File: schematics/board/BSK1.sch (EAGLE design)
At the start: 29 parts

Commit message: Сделаны платы CROSSnew, SPIDERnew, BSK2
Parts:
- removed BSK3: (no value), pinheadCS:PINHD-1X8
- added BKU: (no value), pinheadCS:PINHD-1X20
- added CMD: KCONNECTQUAD, CanCubeSat:KCONNECTQUAD
- added JP1, JP2, JP3, JP4, JP5, JP6: (no value), pinheadCS:PINHD-2X10
- added U$16, U$17, U$6, U$7: GRAFITGRAFIT3_1, CanCubeSat:GRAFITGRAFIT3_1
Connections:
- removed net B5-KHEAT: R8.1, U$8.G
- removed net B5-KVCC: R94.2, R95.2, U$5.AN1, U$5.AN2
- removed net B5-ROZE: R14.1, U$13.G
- removed net KEM7: BSK3.3
- removed net KEM8: BSK3.2
- removed net KHEAT4: BSK3.4
- removed net KVCC4: BSK3.5
- new net 3V3: BKU.8, JP1.9, JP2.9, JP3.9, JP4.9, JP5.9, JP6.9
- new net B1-CMD: BKU.4, CMD.P$1
- new net B1-KHEAT: BKU.1, R8.1, U$8.G
- new net B1-KVCC: BKU.2, R94.2, R95.2, U$5.AN1, U$5.AN2
- new net B1-ROZE: BKU.3, R14.1, U$13.G
- new net BMS1: JP1.1, JP2.1, JP3.1, JP4.5, JP5.3, JP6.3
- new net BMS2: JP1.2, JP2.2, JP3.2, JP4.6, JP5.4, JP6.4
- new net BMS3: JP1.3, JP2.3, JP3.3, JP4.1, JP5.5, JP6.5
- new net BMS4: JP1.4, JP2.4, JP3.4, JP4.2, JP5.6, JP6.6
- new net BMS5: JP1.5, JP2.5, JP3.5, JP4.3, JP5.1, JP6.1
- new net BMS6: JP1.6, JP2.6, JP3.6, JP4.4, JP5.2, JP6.2
- new net I2CINT: BKU.13
- new net INT: JP1.16, JP2.16, JP3.16, JP4.16, JP5.16, JP6.16
- new net PL1: JP1.17, JP2.17, JP3.17, JP4.17, JP5.17, JP6.17
- new net PL1-KVCC: BKU.15
- new net PL2: JP1.19, JP2.19, JP3.19, JP4.19, JP5.19, JP6.19
- new net PL2-KVCC: BKU.16
- new net PL3: JP1.18, JP2.18, JP3.18, JP4.18, JP5.18, JP6.18
- new net PL3-KVCC: BKU.17
- new net PL4: JP1.20, JP2.20, JP3.20, JP4.20, JP5.20, JP6.20
- new net PL4-KVCC: BKU.18
- new net PL5-KVCC: BKU.19
- new net PL6-KVCC: BKU.20
- new net SCL: BKU.10, JP1.13, JP2.13, JP3.13, JP4.13, JP5.13, JP6.13
- new net SDA: BKU.12, JP1.14, JP2.14, JP3.14, JP4.14, JP5.14, JP6.14
- new net TIME: BKU.14, JP1.15, JP2.15, JP3.15, JP4.15, JP5.15, JP6.15
- net 1W: now also BKU.5, JP1.7, JP2.7, JP3.7, JP4.7, JP5.7, JP6.7; no longer BSK3.6
- net 2: now also U$16.P$1, U$17.P$1, U$6.P$1, U$7.P$1
- net 5V: now also BKU.7, JP1.10, JP2.10, JP3.10, JP4.10, JP5.10, JP6.10; no longer BSK3.7
- net BUS+: now also BKU.6, JP1.8, JP2.8, JP3.8, JP4.8, JP5.8, JP6.8, U$16.P$2, U$17.P$2, U$6.P$2, U$7.P$2; no longer BSK3.8
- net GND: now also BKU.11, BKU.9, JP1.11, JP1.12, JP2.11, JP2.12, JP3.11, JP3.12, JP4.11, JP4.12, JP5.11, JP5.12, JP6.11, JP6.12; no longer BSK3.1
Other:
- moved on the sheet: LAP1, LED6, LED7, R12, R13, R14, R4, R5, R6, R7, R8, R9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

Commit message: Добавлены предохранители в библиотеку
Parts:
- removed U$11, U$12: KCONNECT, CanCubeSat:KCONNECT
- removed U$26: FS8205A+, CanCubeSat:FS8205A+
- added BSK5: (no value), pinheadCS:PINHD-1X8
- added LED-G1, LED-G2, LED-G3, LED-G4, LED-G5, LED-G6: (no value), led:LEDCHIPLED_0603
- added R10, R11, R15, R16, R17, R21, R22, R23: 2k, resistor:R-US_R0603
- added R18, R20, R3: 1M, resistor:R-US_R0603
- added R19: 1k5, resistor:R-US_R0603
- added U$18, U$19, U$20, U$21: KCONNECT, CanCubeSat:KCONNECT
- added U$22: MOCD217M, CanCubeSat:MOCD217M
- added U$23: SI2302CDS, CanCubeSat:SI2302CDS
- added U$27, U$28, U$30: GRAFITGRAFIT3_1, CanCubeSat:GRAFITGRAFIT3_1
- R12, R6: value 2M -> 1M
- R13: value 1k5 -> 1M
- R4, R7: value 2k -> 2M
- U$10, U$9: value KCONNECT -> SI2302CDS; device CanCubeSat:KCONNECT -> CanCubeSat:SI2302CDS
- U$17: value GRAFITGRAFIT3_1 -> FS8205A+; device CanCubeSat:GRAFITGRAFIT3_1 -> CanCubeSat:FS8205A+
- U$5: value MOCD217M -> SI2302CDS; device CanCubeSat:MOCD217M -> CanCubeSat:SI2302CDS
- U$6, U$7: value GRAFITGRAFIT3_1 -> SI2302CDS; device CanCubeSat:GRAFITGRAFIT3_1 -> CanCubeSat:SI2302CDS
- renumbered LAP1 to LED_Y, LED6 to LED_B1, LED7 to LED_R, R94 to R1, R95 to R2, U$13 to U$25, U$14 to U$24, U$16 to U$29
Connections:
- removed net 1: R7.2, U$24.GND, U$8.D
- removed net 2: R13.2, U$17.P$1, U$25.D, U$29.P$1, U$6.P$1, U$7.P$1
- removed net I2CINT: BKU.13
- removed net N$26: R5.1, R6.2, U$26.G2
- removed net N$29: LED_R.C, R13.1
- removed net N$31: LED_B1.C, R7.1
- removed net OC1: R9.2, U$5.COL2
- removed net OD1: R5.2, U$5.COL1
- new net 3: R11.2, U$23.D, U$24.GND
- new net 4: R19.2, U$25.D, U$27.P$1, U$28.P$1, U$29.P$1, U$30.P$1
- new net N$2: LED_B1.C, R11.1
- new net N$21: LED-G3.A, R17.2
- new net N$22: LED-G4.A, R21.2
- new net N$23: LED-G5.A, R22.2
- new net N$24: LED-G6.A, R23.2
- new net N$3: LED_R.C, R19.1
- new net N$38: LED-G2.A, R15.2
- new net N$4: LED-G1.A, R16.2
- new net OC2: R3.2, U$22.COL2
- new net OD2: R5.2, U$22.COL1
- new net PL1-GND: JP1.11, JP1.12, LED-G1.C, U$5.D
- new net PL2-GND: JP2.11, JP2.12, LED-G2.C, U$6.D
- new net PL3-GND: JP3.11, JP3.12, LED-G3.C, U$7.D
- new net PL4-GND: JP4.11, JP4.12, LED-G4.C, U$8.D
- new net PL5-GND: JP5.11, JP5.12, LED-G5.C, U$9.D
- new net PL6-GND: JP6.11, JP6.12, LED-G6.C, U$10.D
- new net TIME-ES: BKU.13, BSK5.8
- net 3V3: now also BSK5.3
- net 5V: now also BSK5.2, R10.1, R15.1, R16.1, R17.1, R21.1, R22.1, R23.1; no longer R4.1
- net B1-KHEAT: now also R18.1, U$23.G; no longer R8.1, U$8.G
- net B1-KVCC: now also U$22.AN1, U$22.AN2; no longer U$5.AN1, U$5.AN2
- net B1-ROZE: now also R20.1; no longer R14.1
- net BUS+: now also R4.1, R7.2, U$27.P$2, U$28.P$2, U$30.P$2; no longer R12.2, R6.1, U$17.P$2, U$6.P$2, U$7.P$2
- net BUS+2: now also U$18.P$1; no longer U$9.P$1
- net BUS+3: now also U$20.P$1; no longer U$11.P$1
- net BUS-: now also U$17.S2, U$22.EM1; no longer U$26.S2, U$5.EM1
- net BUS-2: now also U$19.P$1; no longer U$10.P$1
- net BUS-3: now also U$21.P$1; no longer U$12.P$1
- net GND: now also BSK5.1, BSK5.4, BSK5.6, DS18B20Z.HEAT, R12.2, R13.2, R18.2, R20.2, R6.2, R9.2, U$10.S, U$17.HEAT, U$17.S1, U$22.CAT1, U$22.CAT2, U$22.EM2, U$23.S, U$5.S, U$6.S, U$7.S, U$9.S; no longer JP1.11, JP1.12, JP2.11, JP2.12, JP3.11, JP3.12, JP4.11, JP4.12, JP5.11, JP5.12, JP6.11, JP6.12, U$26.S1, U$5.CAT1, U$5.CAT2, U$5.EM2
- net N$1: now also R4.2, R5.1, U$17.G2; no longer DS18B20Z.HEAT, U$26.HEAT
- net N$27: now also R3.1, R7.1, U$17.G1; no longer R12.1, R9.1, U$26.G1
- net N$28: now also R10.2; no longer R4.2
- net PL1-KVCC: now also R6.1, U$5.G
- net PL2-KVCC: now also R8.1, U$6.G
- net PL3-KVCC: now also R9.1, U$7.G
- net PL4-KVCC: now also R12.1, U$8.G
- net PL5-KVCC: now also R13.1, U$9.G
- net PL6-KVCC: now also R14.1, U$10.G
- net SCL: now also BSK5.5
- net SDA: now also BSK5.7
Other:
- moved on the sheet: R12, R13, R14, R4, R6, R7, R8, R9, U$1, U$2, U$3, U$4

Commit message: Разведена БСК1
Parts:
- added C41: 0,1µ, rcl:C-USC0603
- added R75: R01, rcl:R-US_R2512
- added R76, R77: 10R, resistor:R-US_R0603
- added U$57: INA219AID, CanCubeSat:INA219AID
- BSK5: device pinheadCS:PINHD-1X8 -> pinheadCS:PINHD-1X10
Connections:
- net BUS+1 renamed SP+1
- net BUS+2 renamed SP+3
- net BUS- renamed SP-
- net BUS-1 renamed SP-1
- net BUS-2 renamed SP-2
- net BUS-3 renamed SP-3
- net SCL renamed SCL-TM
- net SDA renamed SDA-TM
- removed net BUS+3: U$20.P$1
- new net N$150: C41.1, R76.2, U$57.A1
- new net N$151: C41.2, R77.2, U$57.A0
- new net SCL-INA: BSK5.9, U$57.VS
- new net SDA-INA: BSK5.10, U$57.GND
- new net SP+: R75.1, R77.1, U$20.P$1
- new net SP+2: U$3.P$1
- net 3V3: now also U$57.SCL
- net BUS+: now also R75.2, R76.1; no longer U$3.P$1
- net GND: now also U$57.IN+, U$57.IN-, U$57.SDA

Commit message: Исправлена БСК1
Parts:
- added R24, R25: 2k26, resistor:R-US_R0603
- R1, R2: value 2k26 -> 200k
- R3, R5: value 1M -> 100R
- R4, R7: value 2M -> 100k
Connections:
- new net N$25: R1.2, R24.1, U$22.AN1
- new net N$26: R2.2, R25.1, U$22.AN2
- net 3V3: now also U$57.A0, U$57.VS; no longer U$57.SCL
- net B1-KVCC: now also R24.2, R25.2; no longer R1.2, R2.2, U$22.AN1, U$22.AN2
- net GND: now also U$57.A1, U$57.GND; no longer U$57.IN+, U$57.IN-, U$57.SDA
- net N$150: now also U$57.IN+; no longer U$57.A1
- net N$151: now also U$57.IN-; no longer U$57.A0
- net SCL-INA: now also U$57.SCL; no longer U$57.VS
- net SDA-INA: now also U$57.SDA; no longer U$57.GND

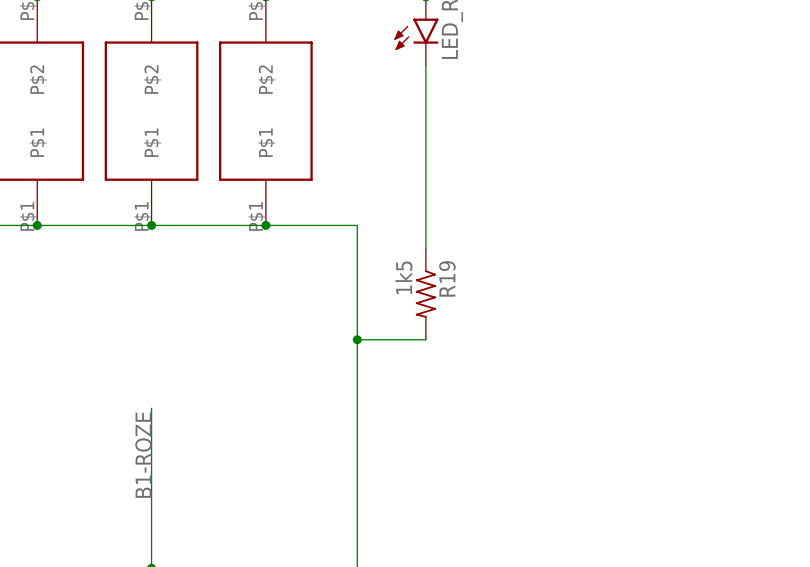
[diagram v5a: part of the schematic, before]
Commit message: Изменен номинал резисторов
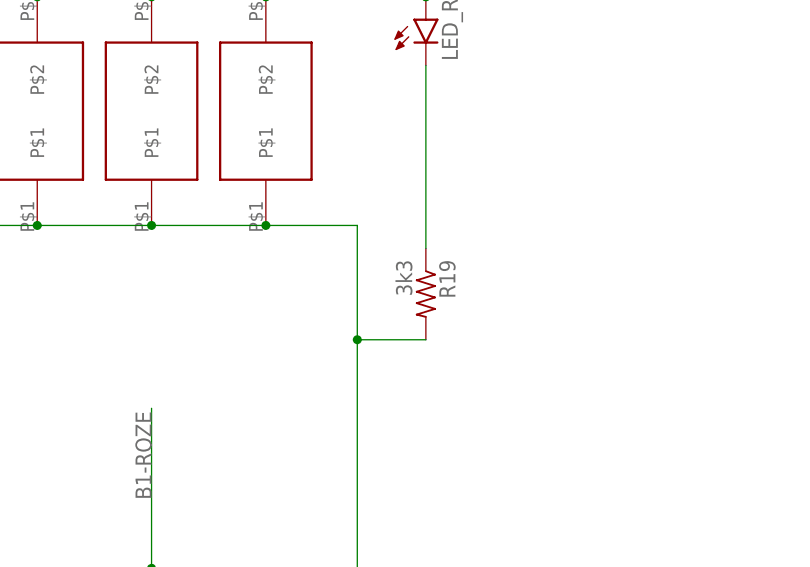
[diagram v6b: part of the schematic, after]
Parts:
- R19: value 1k5 -> 3k3
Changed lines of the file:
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@@
 <part name="R18" library="resistor" deviceset="R-US_" device="R0603" package3d_urn="urn:adsk.eagle:package:23555/3" value="1M"/>
 <part name="U$25" library="CanCubeSat" deviceset="SI2302CDS" device=""/>
-<part name="R19" library="resistor" deviceset="R-US_" device="R0603" package3d_urn="urn:adsk.eagle:package:23555/3" value="1k5"/>
+<part name="R19" library="resistor" deviceset="R-US_" device="R0603" package3d_urn="urn:adsk.eagle:package:23555/3" value="3k3"/>
 <part name="LED_R" library="led" library_urn="urn:adsk.eagle:library:259" deviceset="LED" device="CHIPLED_0603" package3d_urn="urn:adsk.eagle:package:15822/2"/>
 <part name="R20" library="resistor" deviceset="R-US_" device="R0603" package3d_urn="urn:adsk.eagle:package:23555/3" value="1M"/>

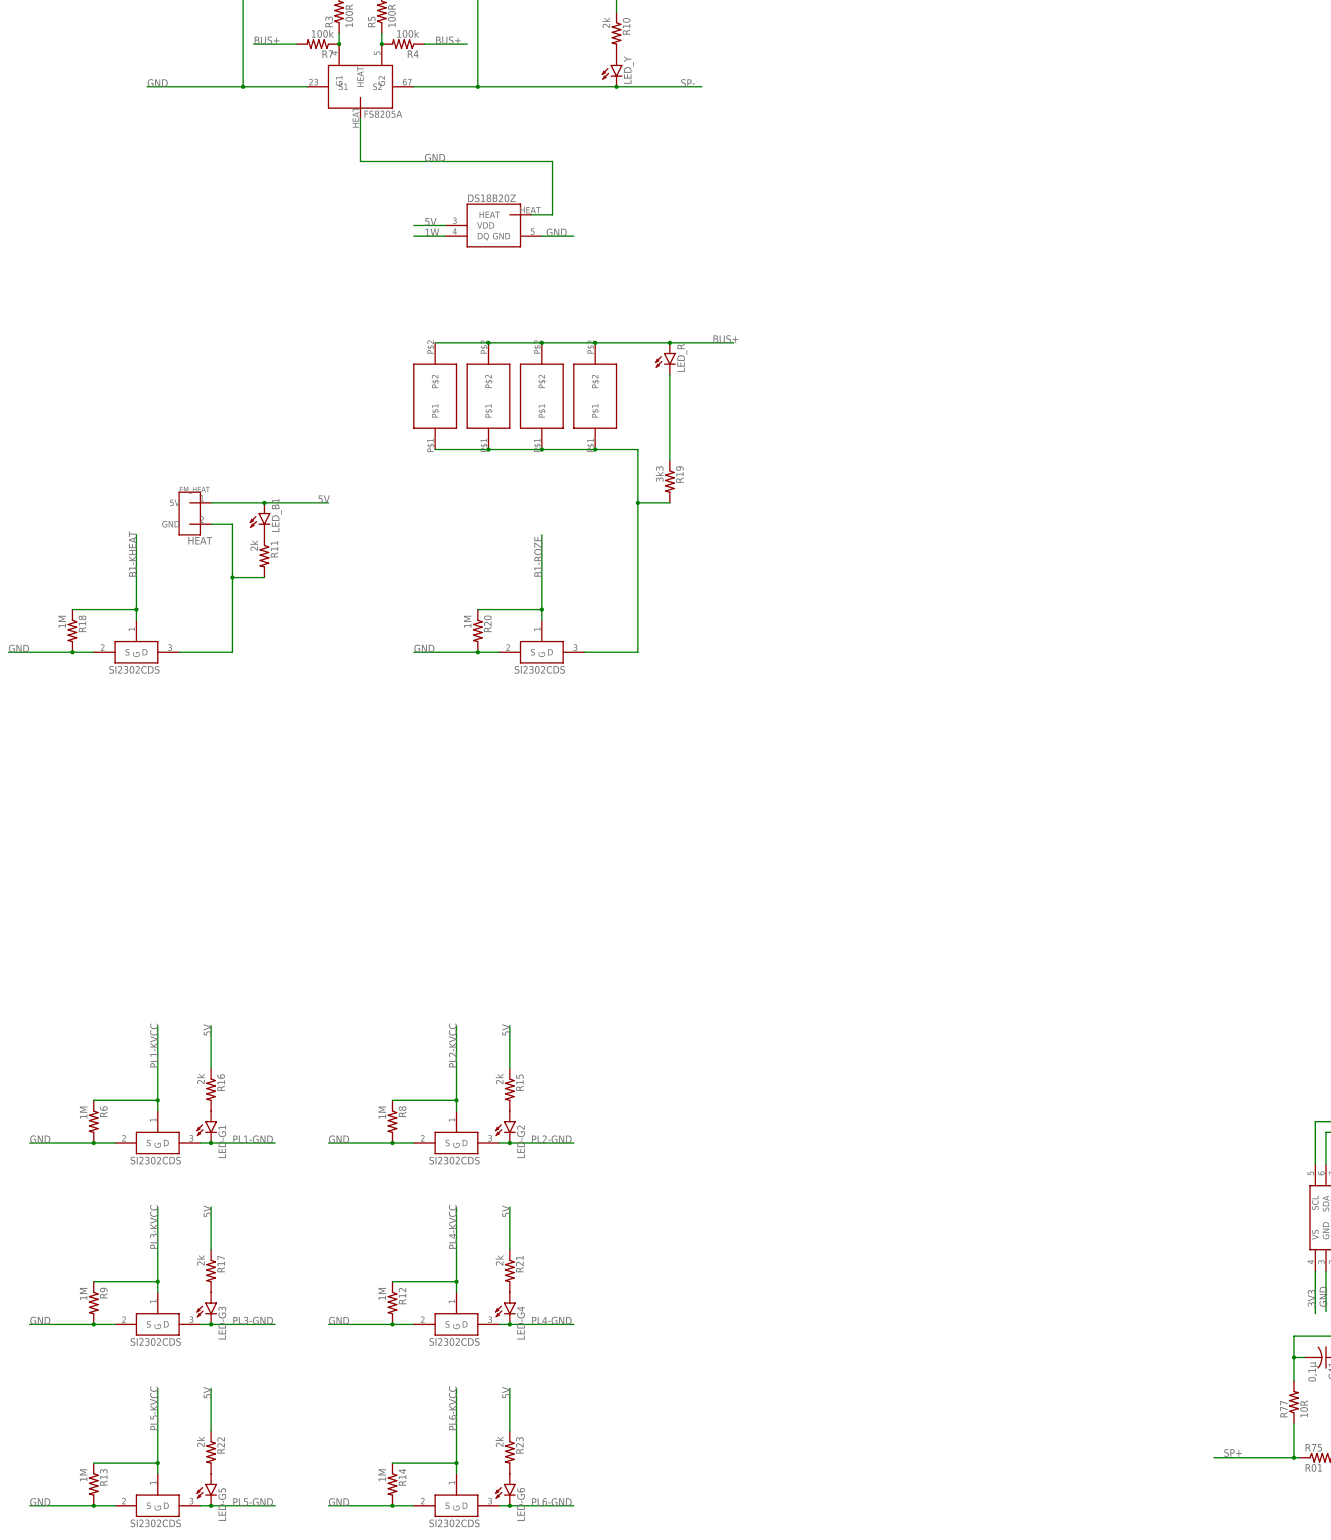
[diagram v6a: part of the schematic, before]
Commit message: Выполнена перетрассировка платы BSK1. Осталось нанести маркировку
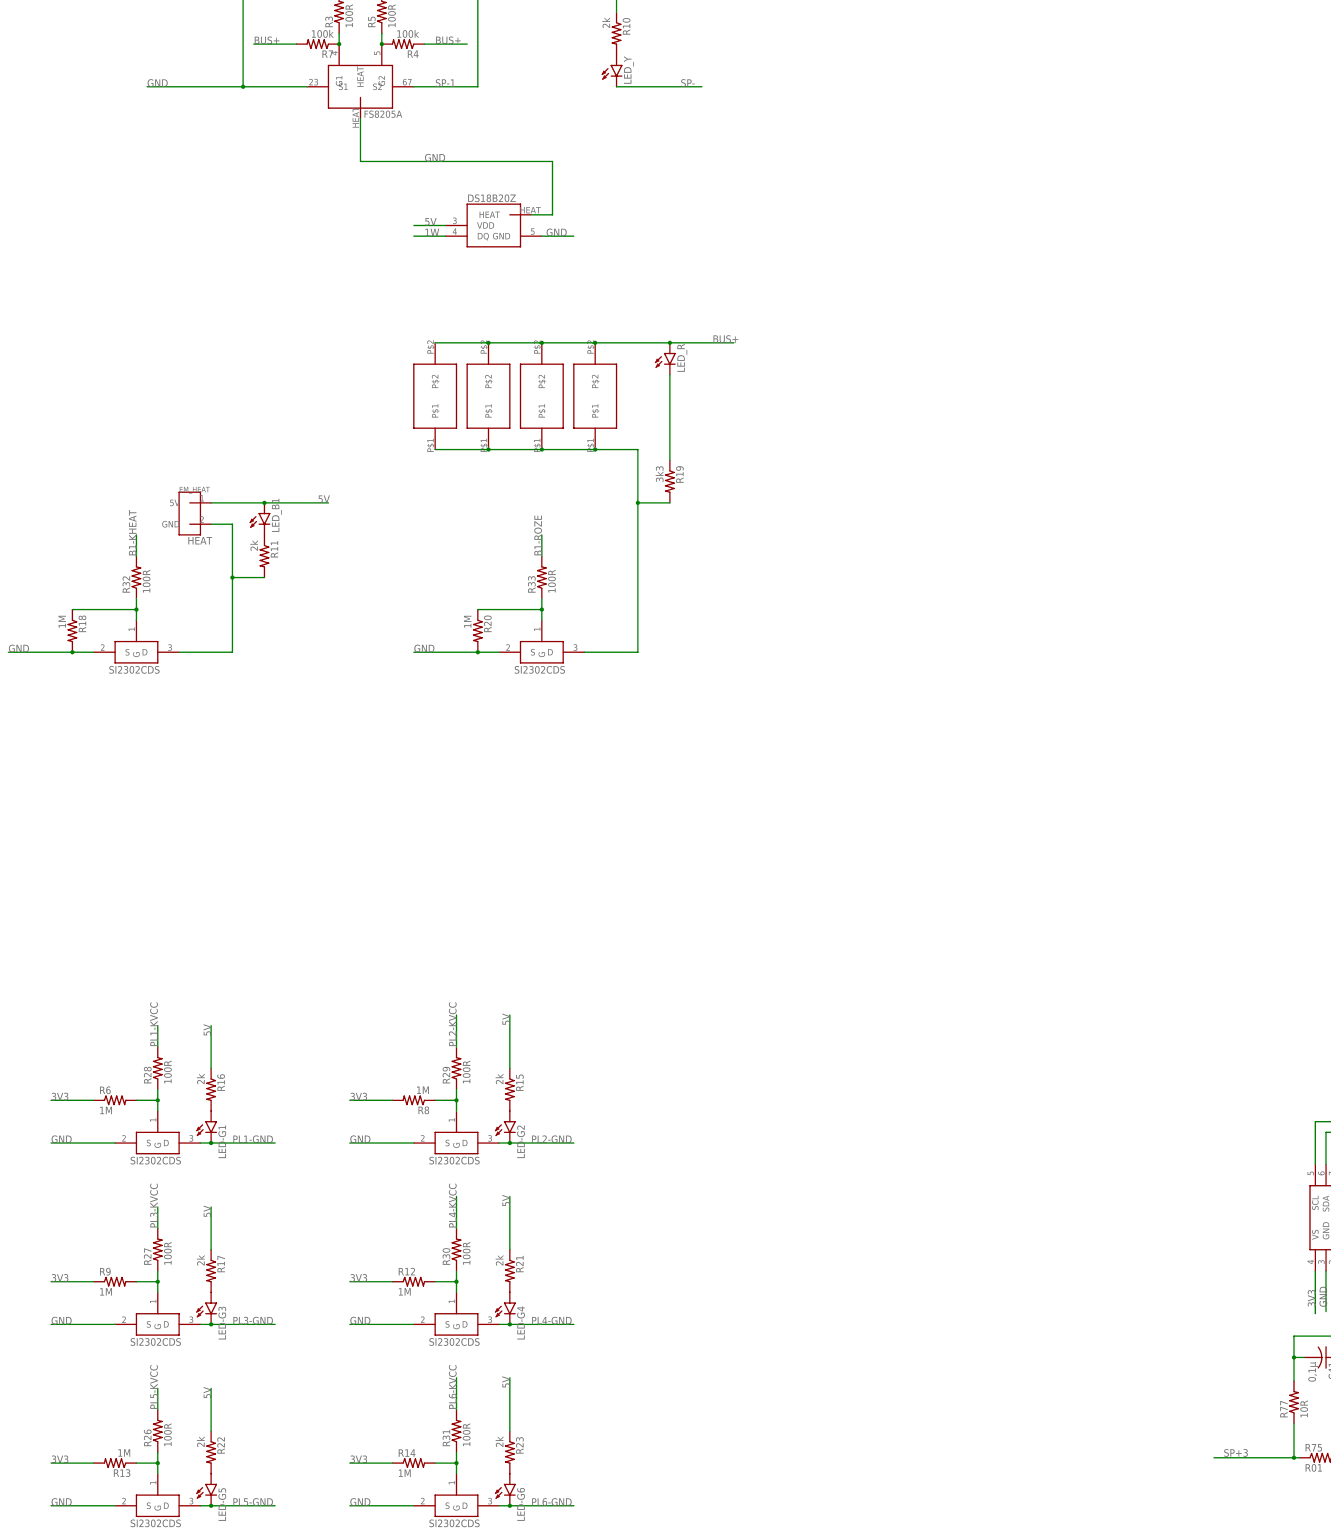
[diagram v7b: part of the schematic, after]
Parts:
- added R26, R27, R28, R29, R30, R31, R32, R33: 100R, resistor:R-US_R0603
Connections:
- new net N$29: R13.1, R26.1, U$9.G
- new net N$30: R27.1, R9.2, U$7.G
- new net N$31: R28.1, R6.2, U$5.G
- new net N$32: R14.2, R31.1, U$10.G
- new net N$34: R29.1, R8.1, U$6.G
- new net N$35: R12.2, R30.1, U$8.G
- new net N$36: R18.1, R32.1, U$23.G
- new net N$37: R20.1, R33.1, U$25.G
- net 3V3: now also R12.1, R13.2, R14.1, R6.1, R8.2, R9.1
- net B1-KHEAT: now also R32.2; no longer R18.1, U$23.G
- net B1-ROZE: now also R33.2; no longer R20.1, U$25.G
- net GND: no longer R12.2, R13.2, R14.2, R6.2, R8.2, R9.2
- net PL1-KVCC: now also R28.2; no longer R6.1, U$5.G
- net PL2-KVCC: now also R29.2; no longer R8.1, U$6.G
- net PL3-KVCC: now also R27.2; no longer R9.1, U$7.G
- net PL4-KVCC: now also R30.2; no longer R12.1, U$8.G
- net PL5-KVCC: now also R26.2; no longer R13.1, U$9.G
- net PL6-KVCC: now also R31.2; no longer R14.1, U$10.G
- net SP+: no longer R75.1, R77.1
- net SP+3: now also R75.1, R77.1
- net SP-: no longer U$17.S2, U$22.EM1
- net SP-1: now also U$17.S2, U$22.EM1
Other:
- moved on the sheet: R12, R13, R14, R6, R8, R9
